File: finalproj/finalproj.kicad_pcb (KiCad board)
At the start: 2 copper layers, 99.2 x 99.6 mm, 52 parts, among them J10 MotorA Out, J11 MotorB Out, J5 Stepper_Motor_Controller, J7 LIDAR_Connector, J9 RPI_UART_Conn, U1 LM1085-12, U2 LM1085-12, U3 LM1085-5.0, U4 LM1085-3.3, U5 L298N

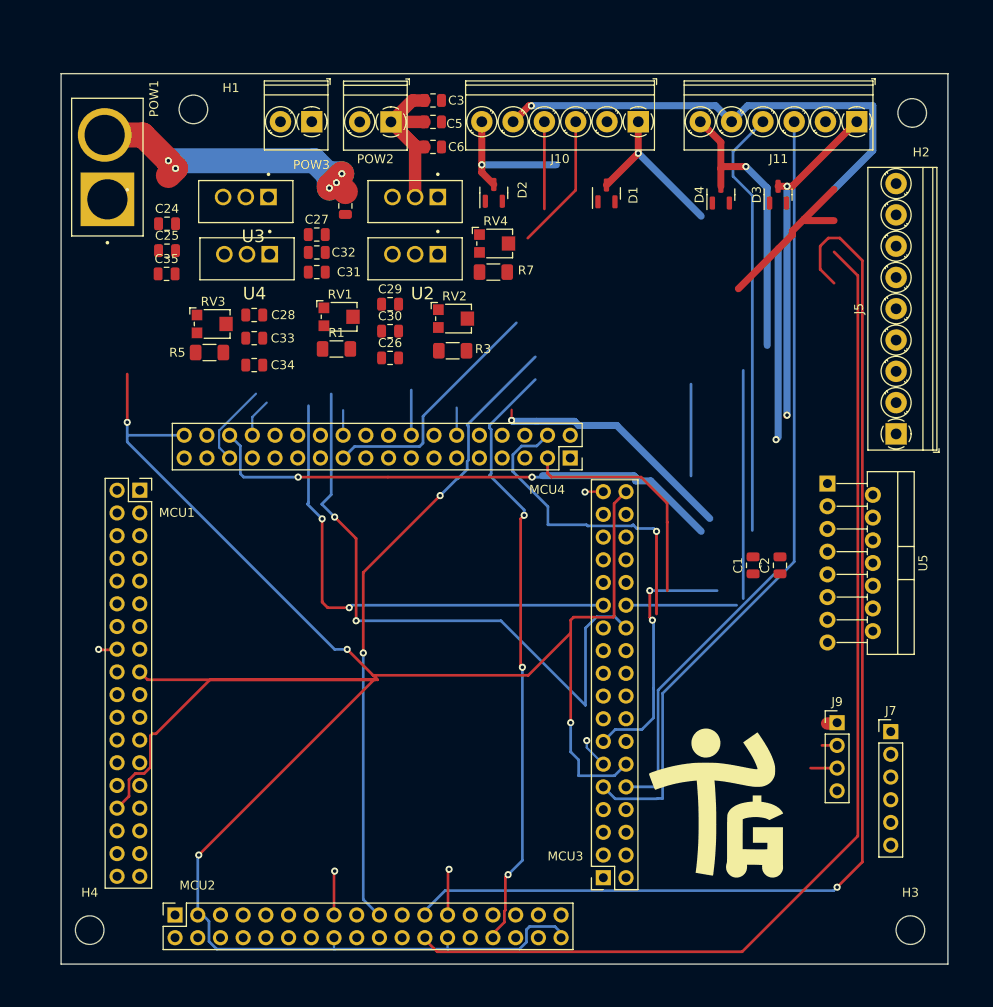
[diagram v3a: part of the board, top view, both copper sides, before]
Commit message: finished pcb2 placement
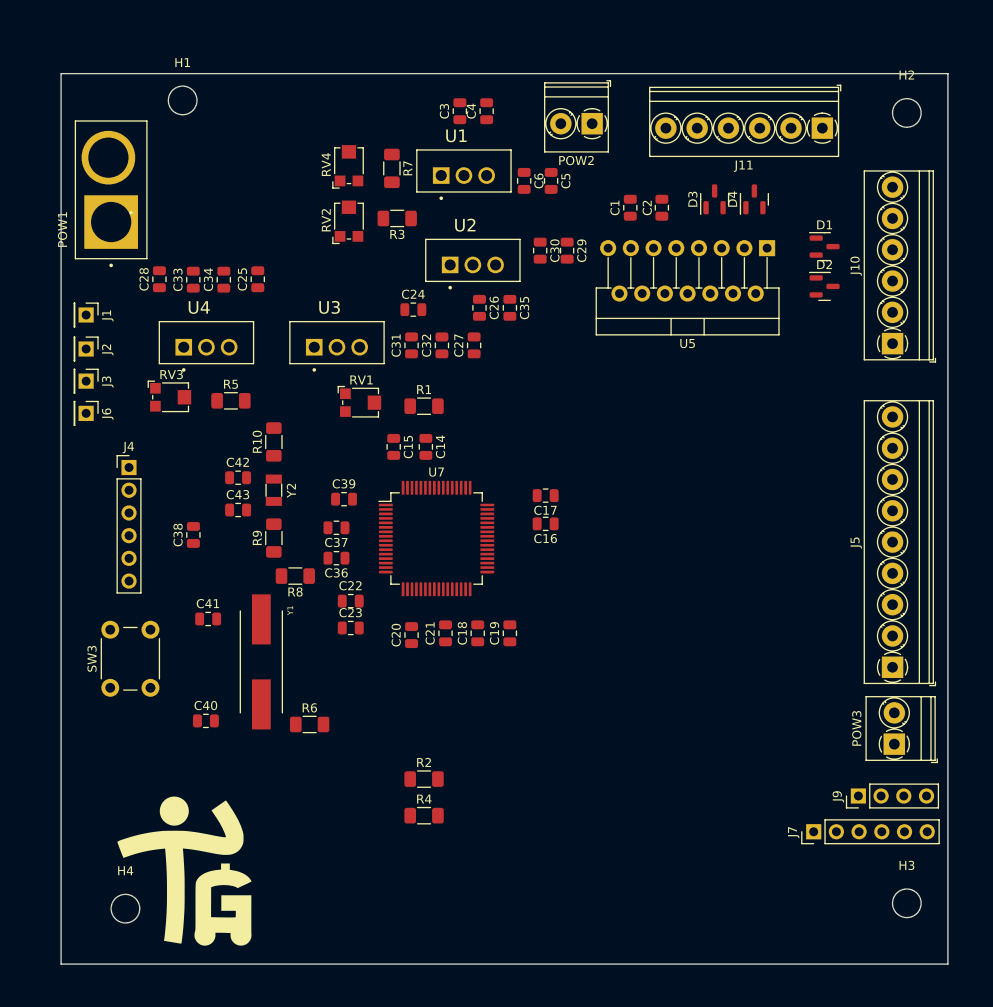
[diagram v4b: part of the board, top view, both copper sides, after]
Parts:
- removed MCU1: MCU_LEFT_CONN, MCU_SOCKETS:MCU1_SOCKET
- removed MCU2: MCU_BOTTOM_CONN, MCU_SOCKETS:MCU2_SOCKETS
- removed MCU3: MCU_RIGHT_CONN, MCU_SOCKETS:MCU3_SOCKETS
- removed MCU4: MCU_TOP_CONN, MCU_SOCKETS:MCU4_SOCKETS
- added C14: 100 nF, Capacitor_SMD:C_0805_2012Metric, F.Cu at (53.4, 54.1)
- added C15: 100 nF, Capacitor_SMD:C_0805_2012Metric, F.Cu at (49.8, 54.1)
- added C16: 100 nF, Capacitor_SMD:C_0805_2012Metric, F.Cu at (66.8, 62.8)
- added C17: 100 nF, Capacitor_SMD:C_0805_2012Metric, F.Cu at (66.8, 59.6)
- added C18: 100 nF, Capacitor_SMD:C_0805_2012Metric, F.Cu at (59.2, 75.0)
- added C19: 100 nF, Capacitor_SMD:C_0805_2012Metric, F.Cu at (62.8, 75.0)
- added C20: 4.7 uF, Capacitor_SMD:C_0805_2012Metric, F.Cu at (51.8, 75.2)
- added C21: 4.7uF, Capacitor_SMD:C_0805_2012Metric, F.Cu at (55.6, 75.0)
- added C22: 100 nF, Capacitor_SMD:C_0805_2012Metric, F.Cu at (45.0, 71.4)
- added C23: 1uF, Capacitor_SMD:C_0805_2012Metric, F.Cu at (45.0, 74.4)
- added C36: 4.7uF, Capacitor_SMD:C_0805_2012Metric, F.Cu at (43.4, 66.6)
- added C37: 4.7uF, Capacitor_SMD:C_0805_2012Metric, F.Cu at (43.4, 63.2)
- added C38: 0.1uF, Capacitor_SMD:C_0805_2012Metric, F.Cu at (27.4, 64.0)
- added C39: 100nF, Capacitor_SMD:C_0805_2012Metric, F.Cu at (44.2, 60.0)
- added C40: 20pF, Capacitor_SMD:C_0805_2012Metric, F.Cu at (28.8, 84.8)
- added C41: 20pF, Capacitor_SMD:C_0805_2012Metric, F.Cu at (29.1, 73.4)
- added C42: 20pF, Capacitor_SMD:C_0805_2012Metric, F.Cu at (32.4, 57.6)
- added C43: 20pF, Capacitor_SMD:C_0805_2012Metric, F.Cu at (32.4, 61.2)
- added J1: Conn_01x01, Connector_PinHeader_2.54mm:PinHeader_1x01_P2.54mm_Vertical, F.Cu at (15.4, 39.4)
- added J2: Conn_01x01, Connector_PinHeader_2.54mm:PinHeader_1x01_P2.54mm_Vertical, F.Cu at (15.4, 43.2)
- added J3: Conn_01x01, Connector_PinHeader_2.54mm:PinHeader_1x01_P2.54mm_Vertical, F.Cu at (15.4, 46.8)
- added J4: Programmer_Conn, Connector_PinHeader_2.54mm:PinHeader_1x06_P2.54mm_Vertical, F.Cu at (20.2, 56.5)
- added J6: Conn_01x01, Connector_PinHeader_2.54mm:PinHeader_1x01_P2.54mm_Vertical, F.Cu at (15.4, 50.4)
- added R10: 0, Resistor_SMD:R_1206_3216Metric_Pad1.30x1.75mm_HandSolder, F.Cu at (36.4, 53.6)
- added R2: 10k, Resistor_SMD:R_1206_3216Metric_Pad1.30x1.75mm_HandSolder, F.Cu at (53.2, 91.3)
- added R4: 10k, Resistor_SMD:R_1206_3216Metric_Pad1.30x1.75mm_HandSolder, F.Cu at (53.2, 95.4)
- added R6: 0, Resistor_SMD:R_1206_3216Metric_Pad1.30x1.75mm_HandSolder, F.Cu at (40.4, 85.2)
- added R8: 0, Resistor_SMD:R_1206_3216Metric_Pad1.30x1.75mm_HandSolder, F.Cu at (38.8, 68.6)
- added R9: 0, Resistor_SMD:R_1206_3216Metric_Pad1.30x1.75mm_HandSolder, F.Cu at (36.4, 64.3)
- added SW3: SW_Push, Button_Switch_THT:SW_PUSH_6mm, F.Cu at (18.1, 81.1)
- added U7: STM32F401RCTx, Package_QFP:LQFP-64_10x10mm_P0.5mm, F.Cu at (54.6, 64.4)
- added Y1: 25 MHz, ABLS-25.000MHZ-B2F-T:XTAL_ABLS-25.000MHZ-B2F-T, F.Cu at (35.0, 78.2)
- added Y2: 32.768 KHz, Crystal:Crystal_SMD_3215-2Pin_3.2x1.5mm, F.Cu at (36.4, 59.0)
- moved POW3 95.4 mm to (105.8, 87.4), turned to 90 degrees
- moved G*** 59.9 mm to (28.0, 102.1)
- moved C1 42.3 mm to (76.3, 27.4)
- moved C2 42.1 mm to (79.8, 27.4)
- moved C35 38.6 mm to (62.8, 38.6), turned to -90 degrees
- moved D2 38.5 mm to (98.0, 36.2), turned to 0 degrees
- moved J10 37.7 mm to (105.6, 42.6), turned to 90 degrees
- moved C24 29.2 mm to (52.0, 38.8)
- moved U5 27.2 mm to (91.6, 31.9), turned to 180 degrees
- moved J5 26.1 mm to (105.6, 78.8)
- moved D1 25.1 mm to (98.0, 31.8), turned to 0 degrees
- moved POW2 22.5 mm to (72.0, 18.0)
- moved C27 21.5 mm to (58.8, 42.8), turned to 90 degrees
- moved C29 20.7 mm to (69.2, 32.2), turned to -90 degrees
- moved U3 19.7 mm to (43.5, 43.0), turned to 0 degrees
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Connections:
- C1 pad 1: +12V -> EXT_12
- C1 pad 2: VSS -> EXT_GND
- C2 pad 1: +12V -> EXT_12
- C2 pad 2: VSS -> EXT_GND
- C24 pad 2: VSS -> EXT_GND
- C25 pad 2: VSS -> EXT_GND
- C26 pad 1: +12V -> EXT_12
- C26 pad 2: VSS -> EXT_GND
- C27 pad 1: +5V -> EXT_5
- C27 pad 2: VSS -> EXT_GND
- C28 pad 1: VDD -> EXT_3.3
- C28 pad 2: VSS -> EXT_GND
- C29 pad 1: +12V -> EXT_12
- C29 pad 2: VSS -> EXT_GND
- C3 pad 2: VSS -> EXT_GND
- C30 pad 1: +12V -> EXT_12
- C30 pad 2: VSS -> EXT_GND
- C31 pad 1: +5V -> EXT_5
- C31 pad 2: VSS -> EXT_GND
- C32 pad 1: +5V -> EXT_5
- C32 pad 2: VSS -> EXT_GND
- C33 pad 1: VDD -> EXT_3.3
- C33 pad 2: VSS -> EXT_GND
- C34 pad 1: VDD -> EXT_3.3
- C34 pad 2: VSS -> EXT_GND
- C35 pad 2: VSS -> EXT_GND
- C4 pad 2: VSS -> EXT_GND
- C5 pad 2: VSS -> EXT_GND
- C6 pad 2: VSS -> EXT_GND
- D1 pad 1: VSS -> EXT_GND
- D1 pad 2: +12V -> EXT_12
- D2 pad 1: VSS -> EXT_GND
- D2 pad 2: +12V -> EXT_12
- D3 pad 1: VSS -> EXT_GND
- D3 pad 2: +12V -> EXT_12
- D4 pad 1: VSS -> EXT_GND
- D4 pad 2: +12V -> EXT_12
- J10 pad 2: VSS -> EXT_GND
- J10 pad 5: +5V -> EXT_5
- J11 pad 2: VSS -> EXT_GND
- J11 pad 5: +5V -> EXT_5
- J5 pad 1: +5V -> EXT_5
- J5 pad 2: VSS -> EXT_GND
- J5 pad 8: +5V -> EXT_5
- J5 pad 9: +5V -> EXT_5
- J7 pad 1: +5V -> EXT_5
- J7 pad 2: VSS -> EXT_GND
- J7 pad 3: VSS -> EXT_GND
- J7 pad 6: VSS -> EXT_GND
- J9 pad 1: +5V -> EXT_5
- J9 pad 4: VSS -> EXT_GND
- POW1 pad 1: VSS -> EXT_GND
- POW2 pad 2: VSS -> EXT_GND
- POW3 pad 1: +12V -> EXT_12
- POW3 pad 2: VSS -> EXT_GND
- R1 pad 1: (no net) -> EXT_5
- R1 pad 2: (no net) -> Net-(U3-GND)
- R3 pad 1: (no net) -> EXT_12
- R3 pad 2: (no net) -> Net-(U2-GND)
- R5 pad 1: (no net) -> EXT_3.3
- R5 pad 2: (no net) -> Net-(U4-GND)
- R7 pad 1: (no net) -> 12V_IC
- R7 pad 2: (no net) -> Net-(U1-GND)
- RV1 pad 1: (no net) -> EXT_GND
- RV1 pad 2: (no net) -> unconnected-(RV1-Pad2)
- RV1 pad 3: (no net) -> Net-(U3-GND)
- RV2 pad 1: (no net) -> EXT_GND
- RV2 pad 2: (no net) -> unconnected-(RV2-Pad2)
- RV2 pad 3: (no net) -> Net-(U2-GND)
- RV3 pad 1: (no net) -> EXT_GND
- RV3 pad 2: (no net) -> unconnected-(RV3-Pad2)
- RV3 pad 3: (no net) -> Net-(U4-GND)
- RV4 pad 1: VSS -> EXT_GND
- U2 pad 1: (no net) -> Net-(U2-GND)
- U2 pad 2: (no net) -> EXT_12
- U2 pad 3: (no net) -> BATTERY_VIN
- U3 pad 2: +5V -> EXT_5
- U4 pad 2: VDD -> EXT_3.3
- U5 pad 1: VSS -> EXT_GND
- U5 pad 15: VSS -> EXT_GND
- U5 pad 4: +5V -> EXT_5
- U5 pad 8: VSS -> EXT_GND
- U5 pad 9: +12V -> EXT_12
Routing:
- net VDD: track 268.3 -> 0.00 mm, vias 4 -> 0
- net STEP_DIR: track 129.3 -> 0.00 mm, vias 1 -> 0
- net STEP_PWM: track 120.7 -> 0.00 mm
- net +5V: track 94.5 -> 0.00 mm, vias 2 -> 0
- net EncoderBFeedback1: track 88.9 -> 0.00 mm
- net EncoderAFeedback1: track 86.4 -> 0.00 mm, vias 2 -> 0
- net EncoderBFeedback2: track 80.6 -> 0.00 mm
- net MotorBIn1: track 71.2 -> 0.00 mm, vias 2 -> 0
- net MotorBIn2: track 67.4 -> 0.00 mm, vias 3 -> 0
- net EncoderAFeedback2: track 64.3 -> 0.00 mm, vias 2 -> 0
- net LIDAR_SDA: track 59.4 -> 0.00 mm, vias 2 -> 0
- net RPI_UART_RX: track 39.0 -> 0.00 mm, vias 1 -> 0
- net MotorBPWM: track 38.9 -> 0.00 mm, vias 2 -> 0
- net MotorAPWM: track 37.9 -> 0.00 mm
- net MotorOutB1: track 37.5 -> 0.00 mm, vias 2 -> 0
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- added copper zone on B.Cu, net EXT_GND
- added copper zone on F.Cu, net EXT_GND
- removed copper zone on B.Cu, net VSS
- removed copper zone on F.Cu, net VSS

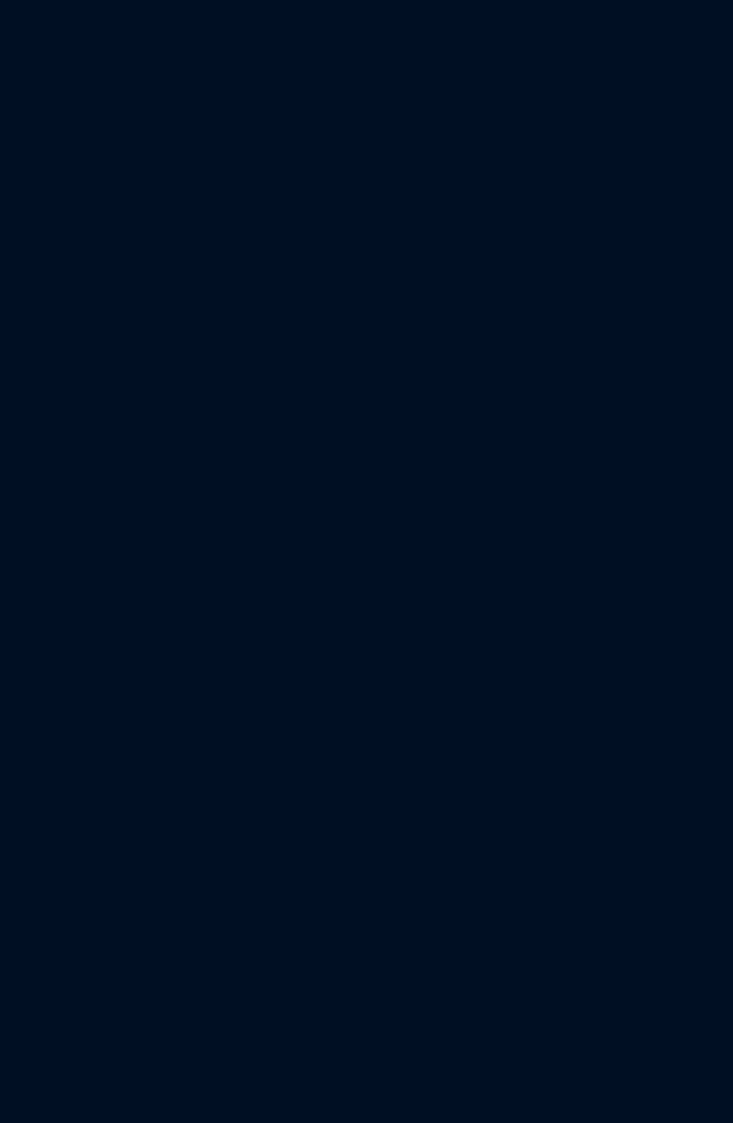
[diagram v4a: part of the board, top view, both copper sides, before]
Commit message: added missing footprint libs, changed footprint lib paths to use ${KIPRJMOD}
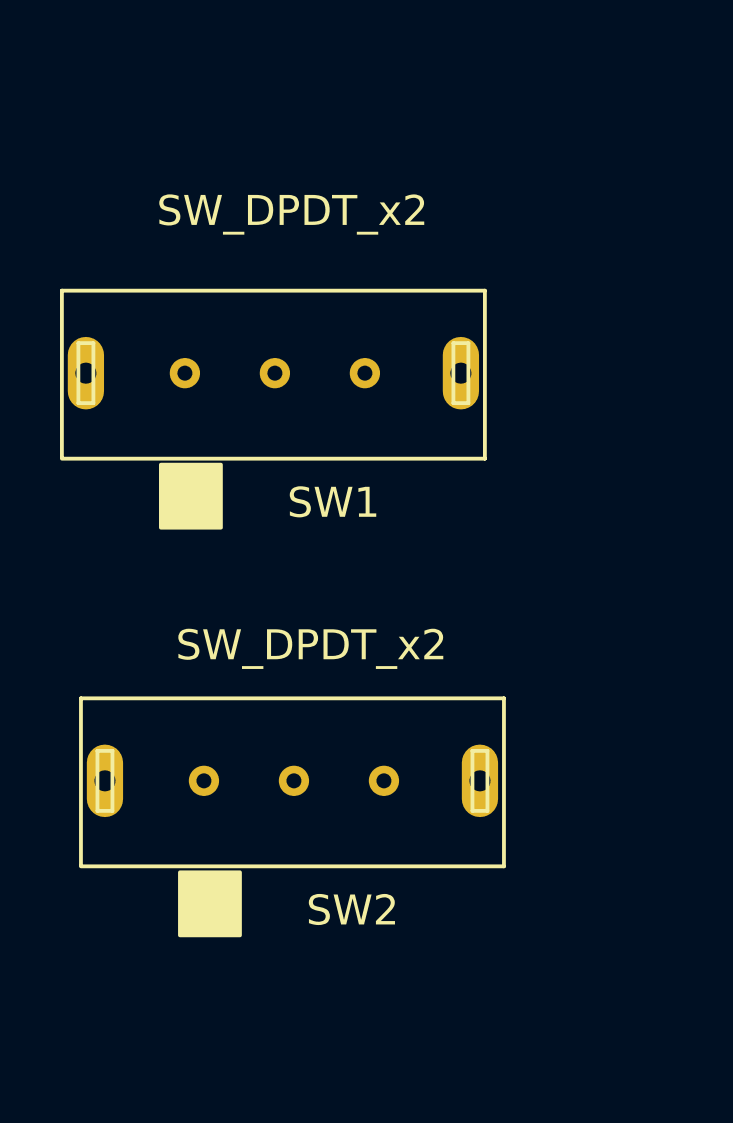
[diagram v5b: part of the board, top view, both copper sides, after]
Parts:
- added SW1: SW_DPDT_x2, Switch_E-Switch_EG1206A:SLIDE-SWITCH, F.Cu at (-26.1, 35.5)
- added SW2: SW_DPDT_x2, Switch_E-Switch_EG1206A:SLIDE-SWITCH, F.Cu at (-25.4, 49.1)
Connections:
- C21 pad 1: (no net) -> EXT_GND
- C21 pad 2: (no net) -> Net-(U7-VCAP1)
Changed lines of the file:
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@@
       (stroke (width 0) (type solid)) (fill solid) (layer "F.SilkS"))
   )
+  (footprint "Switch_E-Switch_EG1206A:SLIDE-SWITCH" (layer "F.Cu")
+    (at -26.062 35.51)
+    (property "Sheetfile" "finalproj.kicad_sch")
+    (property "Sheetname" "")
+    (property "ki_description" "Switch, dual pole double throw, separate symbols")
+    (property "ki_keywords" "switch dual-pole double-throw DPDT spdt ON-ON")
+    (attr through_hole)
+    (fp_text reference "SW1" (at 8.255 3.175) (layer "F.SilkS")
+        (effects (font (size 1 1) (thickness 0.15)))
+    )
+    (fp_text value "SW_DPDT_x2" (at 6.885 -6.554) (layer "F.SilkS")
+        (effects (font (size 1 1) (thickness 0.15)))
+    )
+    (fp_line (start -0.8 -3.9) (end -0.8 1.65)
+      (stroke (width 0.127) (type solid)) (layer "F.SilkS"))
+    (fp_line (start -0.8 -3.9) (end 13.3 -3.9)
+      (stroke (width 0.127) (type solid)) (layer "F.SilkS"))
+    (fp_line (start -0.8 1.7) (end 13.3 1.7)
+      (stroke (width 0.127) (type solid)) (layer "F.SilkS"))
+    (fp_line (start -0.25 -2.15) (end 0.25 -2.15)
+      (stroke (width 0.127) (type solid)) (layer "F.SilkS"))
+    (fp_line (start -0.25 -0.15) (end -0.25 -2.15)
+      (stroke (width 0.127) (type solid)) (layer "F.SilkS"))
+    (fp_line (start 0.25 -0.15) (end -0.25 -0.15)
+      (stroke (width 0.127) (type solid)) (layer "F.SilkS"))
+    (fp_line (start 0.25 -0.15) (end 0.25 -2.15)
+      (stroke (width 0.127) (type solid)) (layer "F.SilkS"))
+    (fp_line (start 12.25 -2.15) (end 12.25 -0.15)
+      (stroke (width 0.127) (type solid)) (layer "F.SilkS"))
+    (fp_line (start 12.75 -2.15) (end 12.25 -2.15)
+      (stroke (width 0.127) (type solid)) (layer "F.SilkS"))
+    (fp_line (start 12.75 -0.15) (end 12.25 -0.15)
+      (stroke (width 0.127) (type solid)) (layer "F.SilkS"))
+    (fp_line (start 12.75 -0.15) (end 12.75 -2.15)
+      (stroke (width 0.127) (type solid)) (layer "F.SilkS"))
+    (fp_line (start 13.3 1.7) (end 13.3 -3.9)
+      (stroke (width 0.127) (type solid)) (layer "F.SilkS"))
+    (fp_poly
+      (pts
+        (xy 2.5 1.9)
+        (xy 2.5 4)
+        (xy 4.5 4)
+        (xy 4.5 1.9)
+      )
+      (stroke (width 0.127) (type solid)) (fill solid) (layer "F.SilkS"))
+    (pad "1" thru_hole circle (at 3.3 -1.15) (size 1.008 1.008) (drill 0.5) (layers "*.Cu" "*.Mask")
+      (net 10 "EXT_3.3") (pinfunction "A") (pintype "passive"))
+    (pad "2" thru_hole circle (at 6.3 -1.15) (size 1.008 1.008) (drill 0.5) (layers "*.Cu" "*.Mask")
+      (net 27 "Net-(SW1A-B)") (pinfunction "B") (pintype "passive"))
+    (pad "3" thru_hole circle (at 9.3 -1.15) (size 1.008 1.008) (drill 0.5) (layers "*.Cu" "*.Mask")
+      (net 3 "EXT_GND") (pinfunction "C") (pintype "passive"))
+    (pad "4" thru_hole oval (at 0 -1.15) (size 1.208 2.416) (drill 0.7) (layers "*.Cu" "*.Mask"))
+    (pad "5" thru_hole oval (at 12.5 -1.15) (size 1.208 2.416) (drill 0.7) (layers "*.Cu" "*.Mask"))
+  )
   (footprint "Capacitor_SMD:C_0805_2012Metric" (layer "F.Cu")
     (at 29.05 73.4)
@@
     )
   )
+  (footprint "Switch_E-Switch_EG1206A:SLIDE-SWITCH" (layer "F.Cu")
+    (at -25.427 49.099)
+    (property "Sheetfile" "finalproj.kicad_sch")
+    (property "Sheetname" "")
+    (property "ki_description" "Switch, dual pole double throw, separate symbols")
+    (property "ki_keywords" "switch dual-pole double-throw DPDT spdt ON-ON")
+    (attr through_hole)
+    (fp_text reference "SW2" (at 8.255 3.175) (layer "F.SilkS")
+        (effects (font (size 1 1) (thickness 0.15)))
+    )
+    (fp_text value "SW_DPDT_x2" (at 6.885 -5.665) (layer "F.SilkS")
+        (effects (font (size 1 1) (thickness 0.15)))
+    )
+    (fp_line (start -0.8 -3.9) (end -0.8 1.65)
+      (stroke (width 0.127) (type solid)) (layer "F.SilkS"))
+    (fp_line (start -0.8 -3.9) (end 13.3 -3.9)
+      (stroke (width 0.127) (type solid)) (layer "F.SilkS"))
+    (fp_line (start -0.8 1.7) (end 13.3 1.7)
+      (stroke (width 0.127) (type solid)) (layer "F.SilkS"))
+    (fp_line (start -0.25 -2.15) (end 0.25 -2.15)
+      (stroke (width 0.127) (type solid)) (layer "F.SilkS"))
+    (fp_line (start -0.25 -0.15) (end -0.25 -2.15)
+      (stroke (width 0.127) (type solid)) (layer "F.SilkS"))
+    (fp_line (start 0.25 -0.15) (end -0.25 -0.15)
+      (stroke (width 0.127) (type solid)) (layer "F.SilkS"))
+    (fp_line (start 0.25 -0.15) (end 0.25 -2.15)
+      (stroke (width 0.127) (type solid)) (layer "F.SilkS"))
+    (fp_line (start 12.25 -2.15) (end 12.25 -0.15)
+      (stroke (width 0.127) (type solid)) (layer "F.SilkS"))
+    (fp_line (start 12.75 -2.15) (end 12.25 -2.15)
+      (stroke (width 0.127) (type solid)) (layer "F.SilkS"))
+    (fp_line (start 12.75 -0.15) (end 12.25 -0.15)
+      (stroke (width 0.127) (type solid)) (layer "F.SilkS"))
+    (fp_line (start 12.75 -0.15) (end 12.75 -2.15)
+      (stroke (width 0.127) (type solid)) (layer "F.SilkS"))
+    (fp_line (start 13.3 1.7) (end 13.3 -3.9)
+      (stroke (width 0.127) (type solid)) (layer "F.SilkS"))
+    (fp_poly
+      (pts
+        (xy 2.5 1.9)
+        (xy 2.5 4)
+        (xy 4.5 4)
+        (xy 4.5 1.9)
+      )
+      (stroke (width 0.127) (type solid)) (fill solid) (layer "F.SilkS"))
+    (pad "1" thru_hole circle (at 3.3 -1.15) (size 1.008 1.008) (drill 0.5) (layers "*.Cu" "*.Mask")
+      (net 10 "EXT_3.3") (pinfunction "A") (pintype "passive"))
+    (pad "2" thru_hole circle (at 6.3 -1.15) (size 1.008 1.008) (drill 0.5) (layers "*.Cu" "*.Mask")
+      (net 23 "Net-(SW2A-B)") (pinfunction "B") (pintype "passive"))
+    (pad "3" thru_hole circle (at 9.3 -1.15) (size 1.008 1.008) (drill 0.5) (layers "*.Cu" "*.Mask")
+      (net 3 "EXT_GND") (pinfunction "C") (pintype "passive"))
+    (pad "4" thru_hole oval (at 0 -1.15) (size 1.208 2.416) (drill 0.7) (layers "*.Cu" "*.Mask"))
+    (pad "5" thru_hole oval (at 12.5 -1.15) (size 1.208 2.416) (drill 0.7) (layers "*.Cu" "*.Mask"))
+  )
   (footprint "MountingHole:MountingHole_3.2mm_M3" (layer "F.Cu")
     (at 107.2 16.8)
@@
       (stroke (width 0.1) (type solid)) (layer "F.Fab"))
     (pad "1" smd roundrect (at -0.95 0 90) (size 1 1.45) (layers "F.Cu" "F.Paste" "F.Mask") (roundrect_rratio 0.25)
-      (pintype "passive"))
+      (net 3 "EXT_GND") (pintype "passive"))
     (pad "2" smd roundrect (at 0.95 0 90) (size 1 1.45) (layers "F.Cu" "F.Paste" "F.Mask") (roundrect_rratio 0.25)
-      (pintype "passive"))
+      (net 11 "Net-(U7-VCAP1)") (pintype "passive"))
     (model "${KICAD6_3DMODEL_DIR}/Capacitor_SMD.3dshapes/C_0805_2012Metric.wrl"
       (offset (xyz 0 0 0))
@@
     (fp_circle (center 0 0) (end 3.45 0)
       (stroke (width 0.05) (type solid)) (fill none) (layer "F.CrtYd"))
-    (pad "" np_thru_hole circle (at 0 0) (size 3.2 3.2) (drill 3.2) (layers "F&B.Cu" "*.Mask"))
+    (pad "" np_thru_hole circle (at 0 0) (size 3.2 3.2) (drill 3.2) (layers "*.Cu" "*.Mask"))
   )
   (footprint "Resistor_SMD:R_1206_3216Metric_Pad1.30x1.75mm_HandSolder" (layer "F.Cu")
